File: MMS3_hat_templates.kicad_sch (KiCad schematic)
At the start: 12 parts, among them U4 AMS1117

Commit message: Scheme
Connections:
- no-connect marks 2 -> 14
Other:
- added sheet Buck Regulator (BuckRegulator.kicad_sch)
- added sheet CH32V003 (CH32V003.kicad_sch)
- added sheet LEDController (LEDController.kicad_sch)
- added sheet LED_IC (LED_IC.kicad_sch)
- added sheet LED_uC (LED_uC.kicad_sch)

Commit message: Schematic
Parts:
- renumbered C16 to C1, C18 to C2, U4 to U1
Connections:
- no-connect marks 14 -> 8
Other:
- removed sheet LED_uC
- added sheet LEDController1 (LEDController.kicad_sch)
- added sheet LEDController2 (LEDController.kicad_sch)
- sheet LEDController ports: added B, G, R; removed none
- sheet LED_IC ports: added LED0, LED1, LED2, LED3, LED4, LED5; removed none

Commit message: reviev by Wojtek
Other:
- sheet Buck Regulator ports: added 12V; removed none
- sheet LEDController ports: added U_IN; removed none
- sheet LEDController1 ports: added U_IN; removed none
- sheet LEDController2 ports: added U_IN; removed none
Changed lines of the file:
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@@
 	(wire
 		(pts
-			(xy 207.01 53.34) (xy 214.63 53.34)
+			(xy 184.15 52.07) (xy 191.77 52.07)
 		)
 		(stroke
@@
 	(wire
 		(pts
-			(xy 208.28 30.48) (xy 214.63 30.48)
+			(xy 185.42 29.21) (xy 191.77 29.21)
 		)
 		(stroke
@@
 	(wire
 		(pts
-			(xy 208.28 20.32) (xy 214.63 20.32)
+			(xy 185.42 19.05) (xy 191.77 19.05)
 		)
 		(stroke
@@
 	(wire
 		(pts
-			(xy 207.01 48.26) (xy 214.63 48.26)
+			(xy 184.15 46.99) (xy 191.77 46.99)
 		)
 		(stroke
@@
 	(wire
 		(pts
+			(xy 246.38 34.29) (xy 252.73 34.29)
+		)
+		(stroke
+			(width 0)
+			(type default)
+		)
+	)
+	(wire
+		(pts
 			(xy 16.51 176.53) (xy 16.51 180.34)
 		)
@@
 	(wire
 		(pts
-			(xy 208.28 25.4) (xy 214.63 25.4)
+			(xy 185.42 24.13) (xy 191.77 24.13)
 		)
 		(stroke
@@
 	(wire
 		(pts
+			(xy 184.15 60.96) (xy 191.77 60.96)
+		)
+		(stroke
+			(width 0)
+			(type default)
+		)
+	)
+	(wire
+		(pts
 			(xy 52.07 140.97) (xy 54.61 140.97)
 		)
@@
 	(wire
 		(pts
-			(xy 52.07 130.81) (xy 72.39 130.81)
+			(xy 52.07 130.81) (xy 81.28 130.81)
 		)
 		(stroke
@@
 		)
 	)
+	(wire
+		(pts
+			(xy 129.54 130.81) (xy 139.7 130.81)
+		)
+		(stroke
+			(width 0)
+			(type default)
+		)
+	)
 	(bus
 		(pts
@@
 	(wire
 		(pts
+			(xy 185.42 33.02) (xy 191.77 33.02)
+		)
+		(stroke
+			(width 0)
+			(type default)
+		)
+	)
+	(wire
+		(pts
 			(xy 157.48 181.61) (xy 157.48 185.42)
 		)
@@
 	(wire
 		(pts
-			(xy 207.01 58.42) (xy 214.63 58.42)
+			(xy 184.15 57.15) (xy 191.77 57.15)
 		)
 		(stroke
@@
 	)
 	(label "G1"
-		(at 208.28 25.4 0)
+		(at 185.42 24.13 0)
+		(effects
+			(font
+				(size 1.27 1.27)
+			)
+			(justify left bottom)
+		)
+	)
+	(label "12V"
+		(at 185.42 33.02 0)
 		(effects
 			(font
@@
 	)
 	(label "B1"
-		(at 208.28 30.48 0)
+		(at 185.42 29.21 0)
+		(effects
+			(font
+				(size 1.27 1.27)
+			)
+			(justify left bottom)
+		)
+	)
+	(label "12V"
+		(at 246.38 34.29 0)
 		(effects
 			(font
@@
 	)
 	(label "G2"
-		(at 207.01 53.34 0)
+		(at 184.15 52.07 0)
 		(effects
 			(font
@@
 		)
 	)
+	(label "12V"
+		(at 184.15 60.96 0)
+		(effects
+			(font
+				(size 1.27 1.27)
+			)
+			(justify left bottom)
+		)
+	)
 	(label "R2"
 		(at 172.72 63.5 180)
@@
 	)
 	(label "R2"
-		(at 207.01 48.26 0)
+		(at 184.15 46.99 0)
 		(effects
 			(font
@@
 		)
 	)
+	(label "12V"
+		(at 139.7 130.81 180)
+		(effects
+			(font
+				(size 1.27 1.27)
+			)
+			(justify right bottom)
+		)
+	)
 	(label "R1"
 		(at 223.52 138.43 0)
@@
 	)
 	(label "B2"
-		(at 207.01 58.42 0)
+		(at 184.15 57.15 0)
 		(effects
 			(font
@@
 	)
 	(label "R1"
-		(at 208.28 20.32 0)
+		(at 185.42 19.05 0)
 		(effects
 			(font
@@
 	)
 	(sheet
-		(at 72.39 125.73)
+		(at 81.28 125.73)
 		(size 48.26 21.59)
 		(exclude_from_sim no)
@@
 		)
 		(property "Sheetname" "Buck Regulator"
-			(at 72.39 125.0184 0)
+			(at 81.28 125.0184 0)
 			(show_name no)
 			(do_not_autoplace no)
@@
 		)
 		(property "Sheetfile" "BuckRegulator.kicad_sch"
-			(at 72.39 147.9046 0)
+			(at 81.28 147.9046 0)
 			(show_name no)
 			(do_not_autoplace no)
@@
 		)
 		(pin "VIN_BRD" input
-			(at 72.39 130.81 180)
+			(at 81.28 130.81 180)
 			(effects
 				(font
@@
 			)
 		)
+		(pin "12V" input
+			(at 129.54 130.81 0)
+			(effects
+				(font
+					(size 1.27 1.27)
+				)
+				(justify right)
+			)
+		)
 		(instances
 			(project "MMS3_hat_templates"
@@
 			)
 		)
+		(pin "U_IN" input
+			(at 252.73 34.29 180)
+			(effects
+				(font
+					(size 1.27 1.27)
+				)
+				(justify left)
+			)
+		)
 		(instances
 			(project "MMS3_hat_templates"
@@
 	)
 	(sheet
-		(at 214.63 43.18)
+		(at 191.77 41.91)
 		(size 30.48 21.59)
 		(exclude_from_sim no)
@@
 		)
 		(property "Sheetname" "LEDController1"
-			(at 214.63 42.4684 0)
+			(at 191.77 41.1984 0)
 			(show_name no)
 			(do_not_autoplace no)
@@
 		)
 		(property "Sheetfile" "LEDController.kicad_sch"
-			(at 214.63 65.3546 0)
+			(at 191.77 64.0846 0)
 			(show_name no)
 			(do_not_autoplace no)
@@
 		)
 		(pin "B" input
-			(at 214.63 58.42 180)
+			(at 191.77 57.15 180)
 			(effects
 				(font
@@
 		)
 		(pin "G" input
-			(at 214.63 53.34 180)
+			(at 191.77 52.07 180)
 			(effects
 				(font
@@
 		)
 		(pin "R" input
-			(at 214.63 48.26 180)
+			(at 191.77 46.99 180)
+			(effects
+				(font
+					(size 1.27 1.27)
+				)
+				(justify left)
+			)
+		)
+		(pin "U_IN" input
+			(at 191.77 60.96 180)
 			(effects
 				(font
@@
 	)
 	(sheet
-		(at 214.63 15.24)
+		(at 191.77 13.97)
 		(size 30.48 21.59)
 		(exclude_from_sim no)
@@
 		)
 		(property "Sheetname" "LEDController"
-			(at 214.63 14.5284 0)
+			(at 191.77 13.2584 0)
 			(show_name no)
 			(do_not_autoplace no)
@@
 		)
 		(property "Sheetfile" "LEDController.kicad_sch"
-			(at 214.63 37.4146 0)
+			(at 191.77 36.1446 0)
 			(show_name no)
 			(do_not_autoplace no)
@@
 		)
 		(pin "B" input
-			(at 214.63 30.48 180)
+			(at 191.77 29.21 180)
 			(effects
 				(font
@@
 		)
 		(pin "G" input
-			(at 214.63 25.4 180)
+			(at 191.77 24.13 180)
 			(effects
 				(font
@@
 		)
 		(pin "R" input
-			(at 214.63 20.32 180)
+			(at 191.77 19.05 180)
+			(effects
+				(font
+					(size 1.27 1.27)
+				)
+				(justify left)
+			)
+		)
+		(pin "U_IN" input
+			(at 191.77 33.02 180)
 			(effects
 				(font

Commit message: Schematic touchup
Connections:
- no-connect marks 8 -> 5
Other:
- sheet LED_IC ports: added LED6, LED7, LED8; removed none
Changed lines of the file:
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@@
 	)
 	(junction
-		(at 109.22 77.47)
-		(diameter 0)
-		(color 0 0 0 0)
-	)
-	(junction
 		(at 101.6 77.47)
 		(diameter 0)
@@
 	)
 	(no_connect
-		(at 231.14 132.08)
-	)
-	(no_connect
 		(at 231.14 104.14)
 	)
@@
 	)
 	(no_connect
-		(at 231.14 127)
-	)
-	(no_connect
 		(at 231.14 101.6)
 	)
 	(no_connect
-		(at 231.14 129.54)
-	)
-	(no_connect
 		(at 96.52 80.01)
 	)
@@
 	(wire
 		(pts
-			(xy 223.52 148.59) (xy 231.14 148.59)
-		)
-		(stroke
-			(width 0)
-			(type default)
-		)
-	)
-	(wire
-		(pts
 			(xy 92.71 176.53) (xy 102.87 176.53)
 		)
@@
 		)
 	)
-	(bus
+	(wire
 		(pts
-			(xy 109.22 77.47) (xy 116.84 77.47)
+			(xy 92.71 186.69) (xy 92.71 189.23)
 		)
 		(stroke
@@
 	(wire
 		(pts
-			(xy 92.71 186.69) (xy 92.71 189.23)
+			(xy 166.37 60.96) (xy 172.72 60.96)
 		)
 		(stroke
@@
 		)
 	)
-	(wire
+	(bus
 		(pts
-			(xy 166.37 60.96) (xy 172.72 60.96)
+			(xy 96.52 77.47) (xy 101.6 77.47)
 		)
 		(stroke
@@
 		)
 	)
-	(bus
+	(wire
 		(pts
-			(xy 96.52 77.47) (xy 101.6 77.47)
+			(xy 223.52 132.08) (xy 231.14 132.08)
 		)
 		(stroke
@@
 	(wire
 		(pts
-			(xy 246.38 20.32) (xy 252.73 20.32)
+			(xy 172.72 71.12) (xy 166.37 71.12)
 		)
 		(stroke
@@
 	(wire
 		(pts
-			(xy 223.52 146.05) (xy 231.14 146.05)
+			(xy 246.38 20.32) (xy 252.73 20.32)
 		)
 		(stroke
@@
 	(wire
 		(pts
-			(xy 223.52 151.13) (xy 231.14 151.13)
+			(xy 172.72 68.58) (xy 166.37 68.58)
 		)
 		(stroke
@@
 	(wire
 		(pts
-			(xy 172.72 68.58) (xy 166.37 68.58)
+			(xy 223.52 140.97) (xy 231.14 140.97)
 		)
 		(stroke
@@
 	(wire
 		(pts
-			(xy 223.52 140.97) (xy 231.14 140.97)
+			(xy 223.52 127) (xy 231.14 127)
 		)
 		(stroke
@@
 	(wire
 		(pts
+			(xy 223.52 129.54) (xy 231.14 129.54)
+		)
+		(stroke
+			(width 0)
+			(type default)
+		)
+	)
+	(wire
+		(pts
 			(xy 223.52 138.43) (xy 231.14 138.43)
 		)
@@
 	(wire
 		(pts
+			(xy 172.72 76.2) (xy 166.37 76.2)
+		)
+		(stroke
+			(width 0)
+			(type default)
+		)
+	)
+	(wire
+		(pts
 			(xy 127 176.53) (xy 127 177.8)
 		)
@@
 	(wire
 		(pts
+			(xy 172.72 73.66) (xy 166.37 73.66)
+		)
+		(stroke
+			(width 0)
+			(type default)
+		)
+	)
+	(wire
+		(pts
 			(xy 246.38 30.48) (xy 252.73 30.48)
 		)
@@
 		)
 	)
-	(label "R3"
-		(at 246.38 20.32 0)
+	(label "G3"
+		(at 172.72 73.66 180)
 		(effects
 			(font
 				(size 1.27 1.27)
 			)
-			(justify left bottom)
+			(justify right bottom)
 		)
 	)
-	(label "Chainbus{I2C}"
-		(at 116.84 77.47 0)
+	(label "R3"
+		(at 246.38 20.32 0)
 		(effects
 			(font
@@
 	)
 	(label "G2"
-		(at 223.52 148.59 0)
+		(at 223.52 129.54 0)
 		(effects
 			(font
@@
 	)
 	(label "B2"
-		(at 223.52 151.13 0)
+		(at 223.52 132.08 0)
 		(effects
 			(font
@@
 	)
 	(label "R2"
-		(at 223.52 146.05 0)
+		(at 223.52 127 0)
 		(effects
 			(font
@@
 		)
 	)
+	(label "R3"
+		(at 172.72 71.12 180)
+		(effects
+			(font
+				(size 1.27 1.27)
+			)
+			(justify right bottom)
+		)
+	)
 	(label "B2"
 		(at 184.15 57.15 0)
@@
 		)
 	)
+	(label "B3"
+		(at 172.72 76.2 180)
+		(effects
+			(font
+				(size 1.27 1.27)
+			)
+			(justify right bottom)
+		)
+	)
 	(label "Chainbus.SDA"
 		(at 223.52 114.3 180)
@@
 	(sheet
 		(at 135.89 53.34)
-		(size 30.48 20.32)
+		(size 30.48 25.146)
 		(exclude_from_sim no)
 		(in_bom yes)
@@
 		)
 		(property "Sheetfile" "LED_IC.kicad_sch"
-			(at 135.89 74.2446 0)
+			(at 135.89 79.0706 0)
 			(show_name no)
 			(do_not_autoplace no)
@@
 			(effects
 				(font
+					(size 1.27 1.27)
+				)
+				(justify right)
+			)
+		)
+		(pin "LED6" passive
+			(at 166.37 71.12 0)
+			(effects
+				(font
+					(size 1.27 1.27)
+				)
+				(justify right)
+			)
+		)
+		(pin "LED7" passive
+			(at 166.37 73.66 0)
+			(effects
+				(font
+					(size 1.27 1.27)
+				)
+				(justify right)
+			)
+		)
+		(pin "LED8" passive
+			(at 166.37 76.2 0)
+			(effects
+				(font

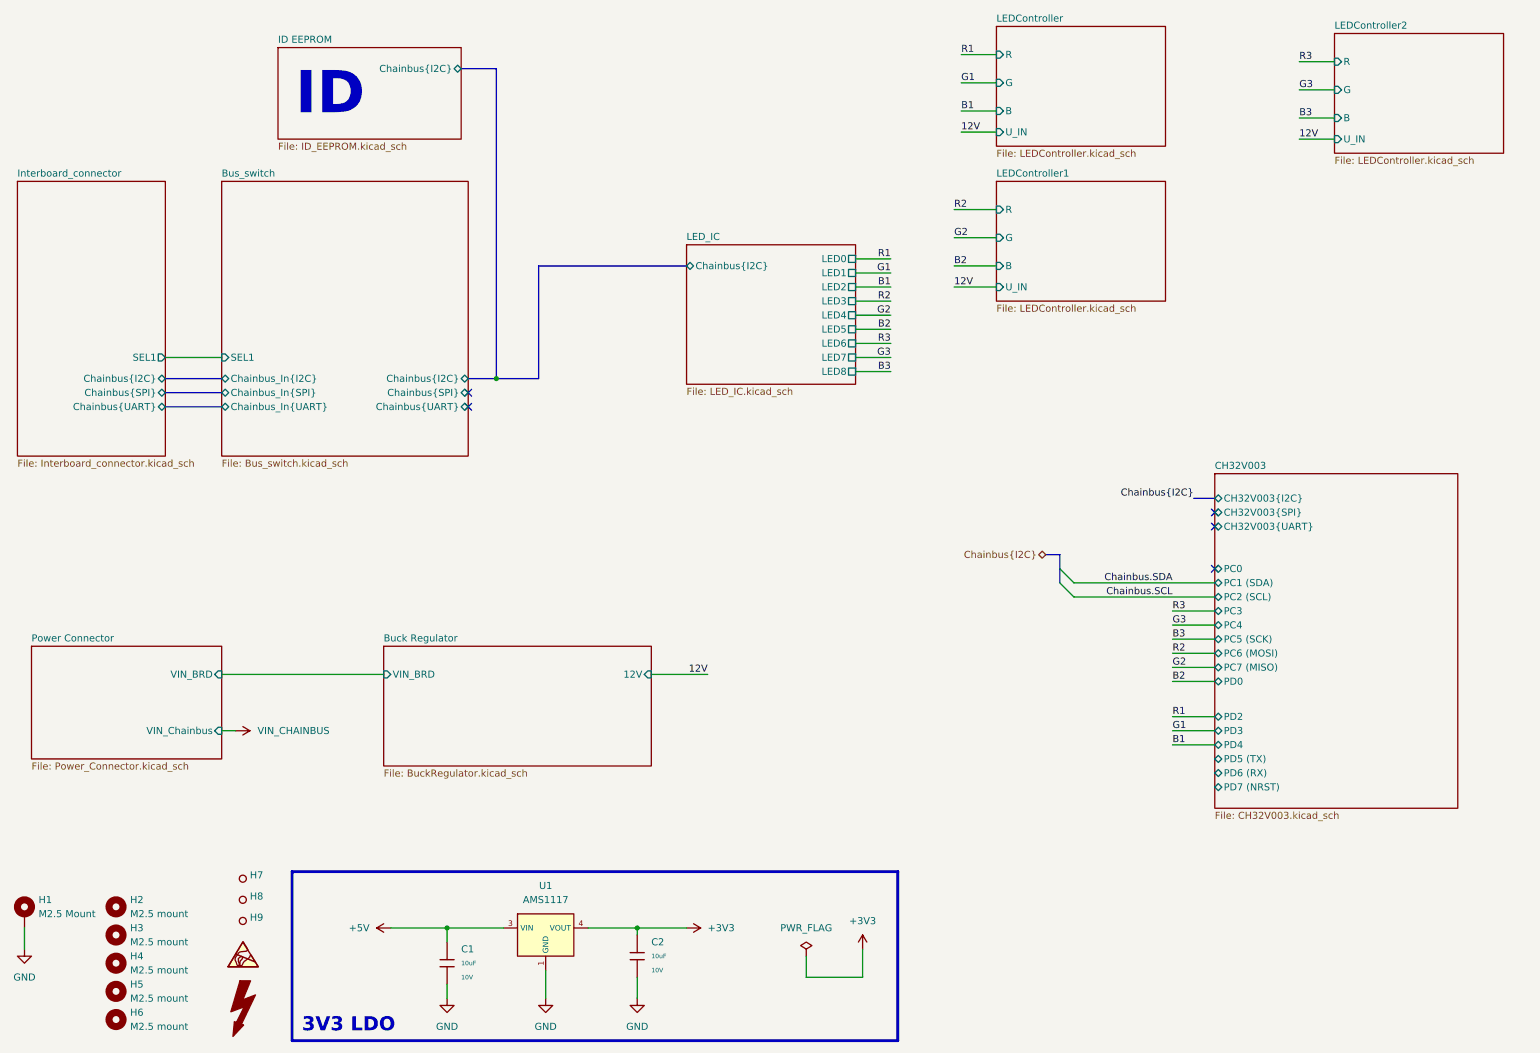
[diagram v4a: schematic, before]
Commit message: PCB design
Hat allows to connect 1 LED tape at a time
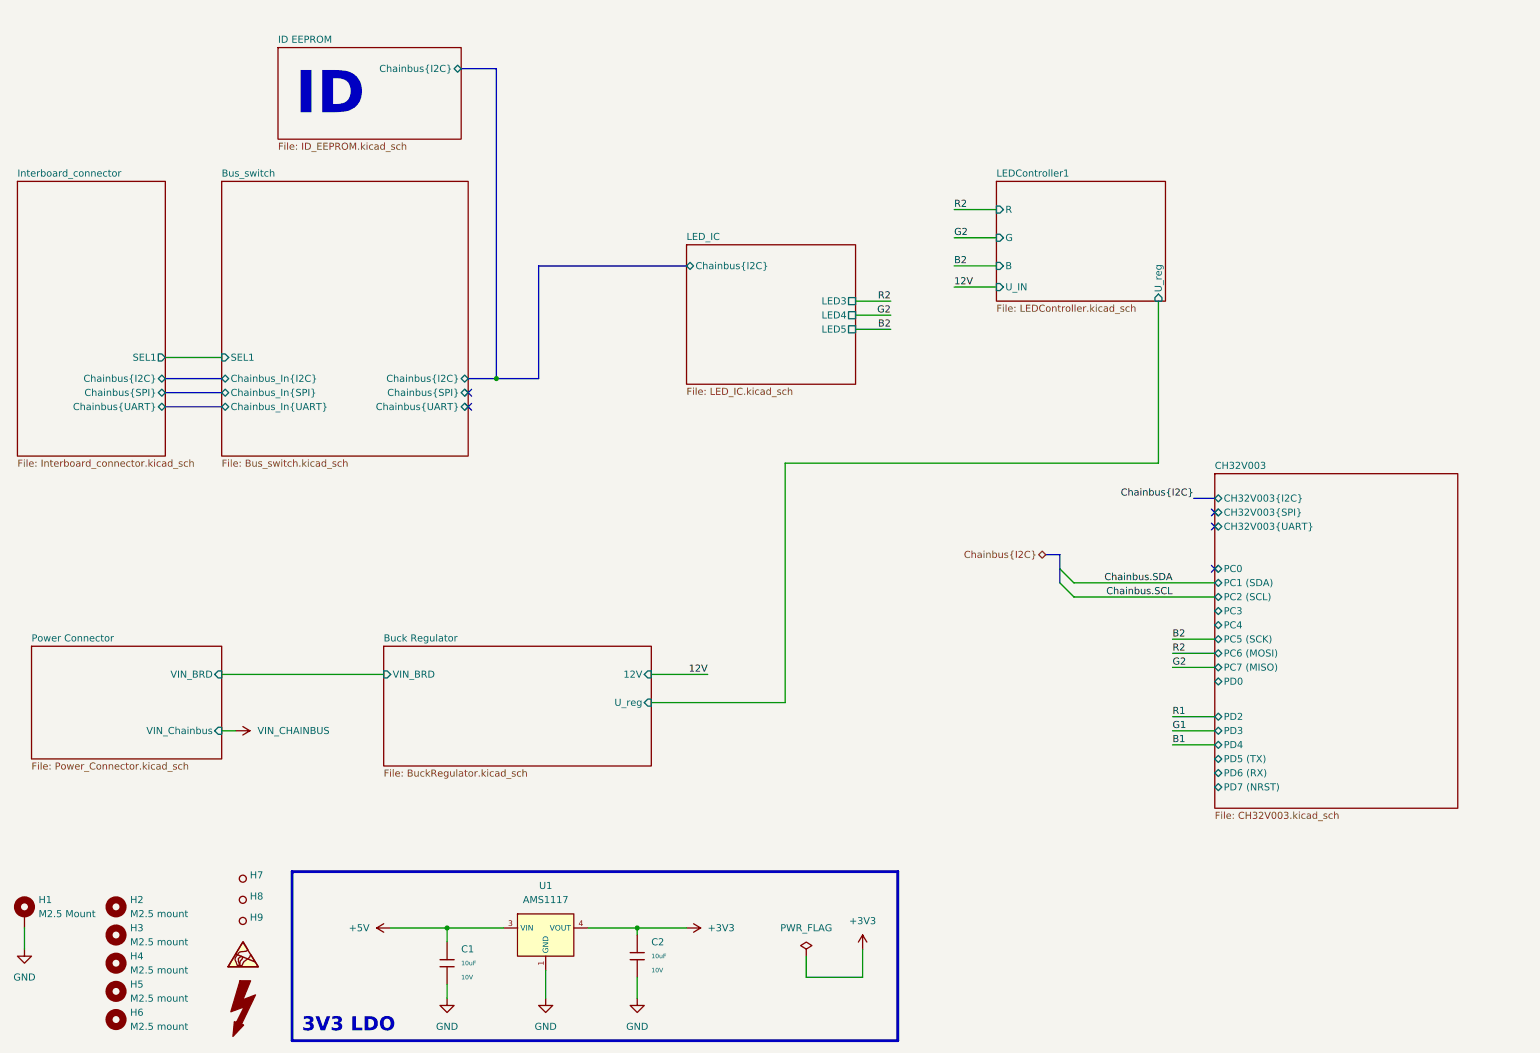
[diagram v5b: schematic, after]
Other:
- removed sheet LEDController
- removed sheet LEDController2
- sheet Buck Regulator ports: added U_reg; removed none
- sheet LEDController1 ports: added U_reg; removed none
- sheet LED_IC ports: added none; removed LED0, LED1, LED2, LED6, LED7, LED8

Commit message: PCB addjustments
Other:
- sheet Buck Regulator ports: added none; removed U_reg
- sheet LEDController1 ports: added none; removed U_reg
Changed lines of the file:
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@@
 	(wire
 		(pts
-			(xy 220.98 92.71) (xy 153.67 92.71)
-		)
-		(stroke
-			(width 0)
-			(type default)
-		)
-	)
-	(wire
-		(pts
 			(xy 92.71 176.53) (xy 102.87 176.53)
 		)
@@
 	(wire
 		(pts
-			(xy 153.67 92.71) (xy 153.67 135.89)
-		)
-		(stroke
-			(width 0)
-			(type default)
-		)
-	)
-	(wire
-		(pts
 			(xy 172.72 68.58) (xy 166.37 68.58)
 		)
@@
 	(wire
 		(pts
-			(xy 153.67 135.89) (xy 129.54 135.89)
-		)
-		(stroke
-			(width 0)
-			(type default)
-		)
-	)
-	(wire
-		(pts
 			(xy 223.52 140.97) (xy 231.14 140.97)
 		)
@@
 		)
 	)
-	(wire
-		(pts
-			(xy 220.98 63.5) (xy 220.98 92.71)
-		)
-		(stroke
-			(width 0)
-			(type default)
-		)
-	)
 	(bus
 		(pts
@@
 			)
 		)
-		(pin "U_reg" input
-			(at 129.54 135.89 0)
-			(effects
-				(font
-					(size 1.27 1.27)
-				)
-				(justify right)
-			)
-		)
 		(instances
 			(project "MMS3_hat_templates"
@@
 			(effects
 				(font
-					(size 1.27 1.27)
-				)
-				(justify left)
-			)
-		)
-		(pin "U_reg" input
-			(at 220.98 63.5 270)
-			(effects
-				(font
